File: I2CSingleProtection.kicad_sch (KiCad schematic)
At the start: 9 parts, among them Q21 NX3008NBKS, Q22 MBT2222ADW1T1

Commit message: v3.1 Updates
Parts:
- C39: renamed from C38; value 10nF -> 10n; symbol Device:C -> Device:C_Small
- R70: renamed from R121; value 10K -> 10k
- R71: renamed from R122; value 10K -> 10k
- R73: renamed from R119; value 100K -> 100k
- R74: renamed from R123; value 200K -> 200k
- R75: renamed from R120; value DNI (0R) -> 0R; now not fitted
- renumbered Q22 to Q12, Q21 to Q13, R118 to R72
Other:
- company: (none) -> Carnegie Mellon University
- title: (none) -> Argus XY Solar Panel

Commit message: Local Stash
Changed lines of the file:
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@@
 			)
 		)
-		(property "Description" "Dual NPN BJT - 2NPN"
+		(property "Description" "600mA IC, 40V Vce, Dual NPN/NPN Transistors, SOT-363"
 			(at 143.51 87.63 0)
 			(effects
@@
 	)
 	(symbol
+		(lib_name "MBT2222ADW1T1_1")
 		(lib_id "Transistor_BJT:MBT2222ADW1T1")
 		(at 143.51 69.85 90)

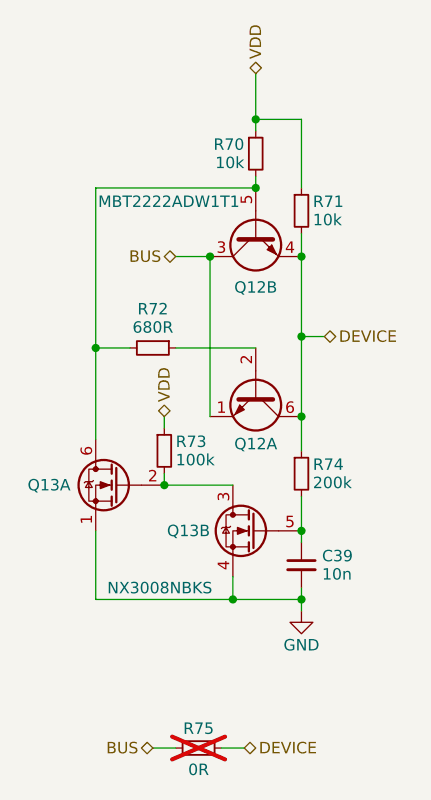
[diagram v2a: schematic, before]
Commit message: Updated access port, added deployment sensor
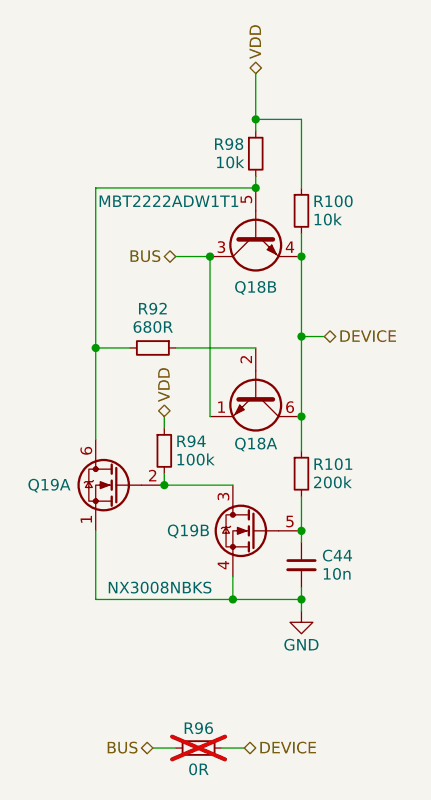
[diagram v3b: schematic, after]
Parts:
- C44: renamed from C39; MPN (none) -> C161232
- Q19: renamed from Q13; MPN (none) -> C3280240; Manufacturer_Name Nexperia USA Inc. -> (none); Manufacturer_Part_Number NX3008NBKS -> (none)
- R100: renamed from R71; MPN (none) -> C2479067
- R101: renamed from R74; MPN (none) -> C118142
- R92: renamed from R72; MPN (none) -> C844802
- R94: renamed from R73; MPN (none) -> C237792
- R96: renamed from R75; now left out of the parts list
- R98: renamed from R70; MPN (none) -> C2479067
- renumbered Q12 to Q18
